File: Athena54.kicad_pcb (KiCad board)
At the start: 4 copper layers, 130.3 x 112.7 mm, 104 parts, among them J1 BATT, J2 HRO_TYPE-C-31-M-12, J3 JTAG_TC2030, J4 RGB, Q1 2N7002, Q2 2N7002, Q3 AO3407, SW1 POWER, SW10 MX Hotswap, SW11 MX Hotswap, SW12 MX Hotswap, SW13 MX Hotswap, SW14 MX Hotswap, SW15 MX Hotswap, SW16 MX Hotswap, SW17 MX Hotswap, SW18 MX Hotswap, SW19 MX Hotswap, SW2 MX Hotswap, SW20 MX Hotswap, SW21 MX Hotswap, SW22 MX Hotswap, SW23 MX Hotswap, SW24 MX Hotswap, SW25 MX Hotswap, SW26 MX Hotswap, SW27 MX Hotswap, SW28 MX Hotswap, SW29 RESET, SW3 MX Hotswap, SW4 MX Hotswap, SW5 MX Hotswap, SW6 MX Hotswap, SW7 MX Hotswap, SW8 MX Hotswap, SW9 MX Hotswap, U1 BQ24075RGT, U2 MAX17048, U3 SRV05-4, U4 MS88SF3

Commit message: fix(schematic): Adjust charging parameters
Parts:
- C6: value 1uF -> 4.7uF
- C7: value 4.7uF -> 1uF
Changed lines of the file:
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@@
       (effects (font (size 0.8 0.8) (thickness 0.15)) (justify mirror))
     )
-    (fp_text value "1uF" (at 0 -1.16) (layer "B.Fab")
+    (fp_text value "4.7uF" (at 0 -1.16) (layer "B.Fab")
       (effects (font (size 1 1) (thickness 0.15)) (justify mirror))
     )
@@
       (effects (font (size 0.8 0.8) (thickness 0.15)) (justify mirror))
     )
-    (fp_text value "4.7uF" (at 0 -1.16) (layer "B.Fab")
+    (fp_text value "1uF" (at 0 -1.16) (layer "B.Fab")
       (effects (font (size 1 1) (thickness 0.15)) (justify mirror))
     )

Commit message: fix(pcb): Update column stagger measurement table
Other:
- board text added: "Pinky2 -> Pinky: 0mm Pinky -> Ring: 5mm Ring -> Middle: 2mm Middle -> Index: 2mm Index -> Index2: 2mm"
- board text removed: "Pinky2 -> Pinky: 0mm Pinky -> Ring: 5mm Ring -> Middle: 1mm Middle -> Index: 2mm Index -> Index2: 2mm"
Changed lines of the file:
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@@
     (fp_line (start 4.47 3.65) (end -4.47 3.65) (layer "B.Fab") (width 0.1))
     (fp_line (start 4.47 -3.65) (end -4.47 -3.65) (layer "B.Fab") (width 0.1))
-    (fp_line (start 4.47 -3.65) (end 4.47 3.65) (layer "F.Fab") (width 0.1))
-    (fp_line (start -4.47 -3.65) (end 4.47 -3.65) (layer "F.Fab") (width 0.1))
     (fp_line (start -4.47 3.65) (end 4.47 3.65) (layer "F.Fab") (width 0.1))
+    (fp_line (start -4.47 -3.65) (end 4.47 -3.65) (layer "F.Fab") (width 0.1))
+    (fp_line (start 4.47 -3.65) (end 4.47 3.65) (layer "F.Fab") (width 0.1))
     (fp_line (start -4.47 -3.65) (end -4.47 3.65) (layer "F.Fab") (width 0.1))
     (pad "" np_thru_hole circle (at 2.89 -2.6 90) (size 0.65 0.65) (drill 0.65) (layers *.Cu *.Mask))
@@
     (effects (font (size 1 1) (thickness 0.2)) (justify left))
   )
-  (gr_text "Pinky2	-> 	Pinky:	0mm\nPinky 	-> 	Ring:	5mm\nRing 	-> 	Middle:	1mm\nMiddle 	-> 	Index:	2mm\nIndex 	-> 	Index2:	2mm\n" (at -13.675 100.025) (layer "Cmts.User")
+  (gr_text "Pinky2	-> 	Pinky:	0mm\nPinky 	-> 	Ring:	5mm\nRing 	-> 	Middle:	2mm\nMiddle 	-> 	Index:	2mm\nIndex 	-> 	Index2:	2mm\n" (at -13.675 100.025) (layer "Cmts.User")
     (effects (font (size 1.5 1.5) (thickness 0.3)) (justify left))
   )

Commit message: fix(schematic): Fix links to footprints
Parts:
- H1, H2, H3, H4, H5: value MountingHole -> 4.3mm
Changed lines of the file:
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@@
       (effects (font (size 1 1) (thickness 0.15)))
     )
-    (fp_text value "MountingHole" (at 0 5.3) (layer "F.Fab")
+    (fp_text value "4.3mm" (at 0 5.3) (layer "F.Fab")
       (effects (font (size 1 1) (thickness 0.15)))
     )
@@
       (effects (font (size 1 1) (thickness 0.15)))
     )
-    (fp_text value "MountingHole" (at 0 5.3) (layer "F.Fab")
+    (fp_text value "4.3mm" (at 0 5.3) (layer "F.Fab")
       (effects (font (size 1 1) (thickness 0.15)))
     )
@@
       (effects (font (size 1 1) (thickness 0.15)))
     )
-    (fp_text value "MountingHole" (at 0 5.3 90) (layer "F.Fab")
+    (fp_text value "4.3mm" (at 0 5.3 90) (layer "F.Fab")
       (effects (font (size 1 1) (thickness 0.15)))
     )
@@
       (effects (font (size 1 1) (thickness 0.15)))
     )
-    (fp_text value "MountingHole" (at 0 5.3) (layer "F.Fab")
+    (fp_text value "4.3mm" (at 0 5.3) (layer "F.Fab")
       (effects (font (size 1 1) (thickness 0.15)))
     )
@@
       (effects (font (size 1 1) (thickness 0.15)))
     )
-    (fp_text value "MountingHole" (at 0 5.3) (layer "F.Fab")
+    (fp_text value "4.3mm" (at 0 5.3) (layer "F.Fab")
       (effects (font (size 1 1) (thickness 0.15)))
     )

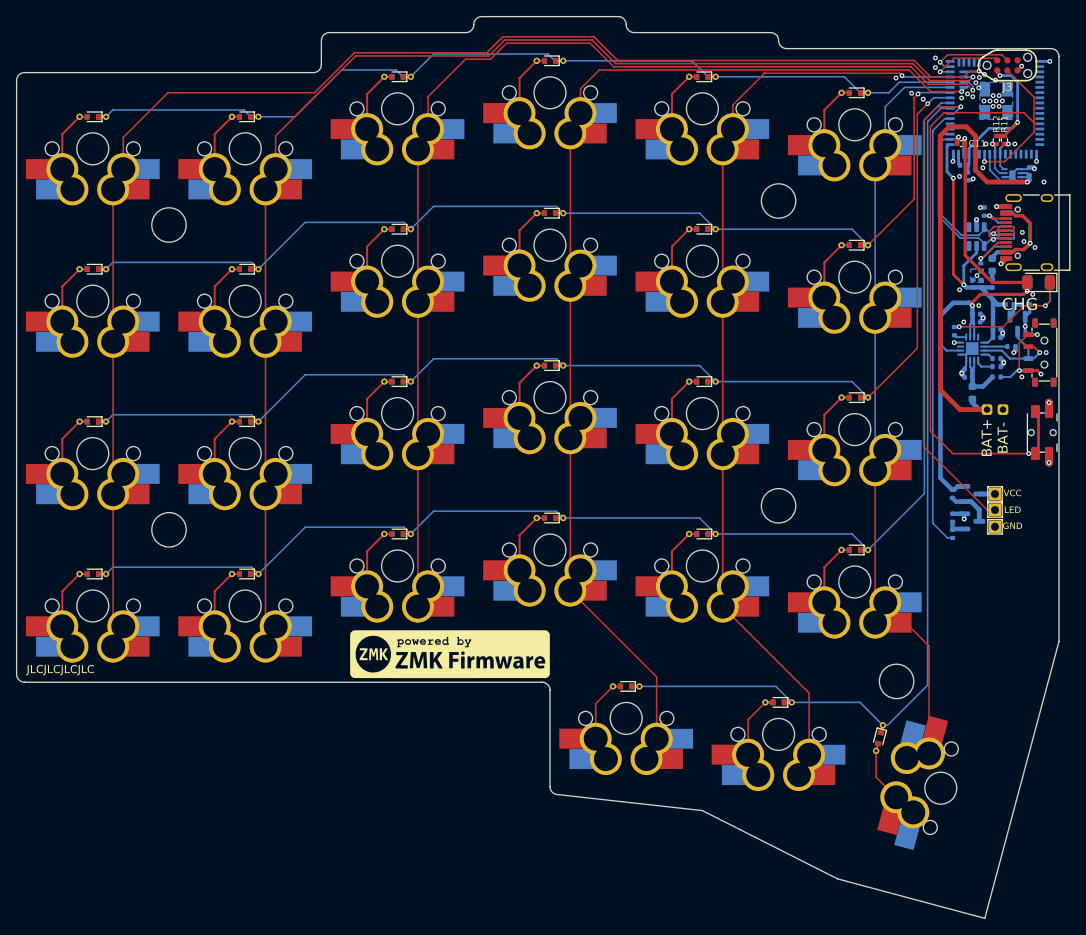
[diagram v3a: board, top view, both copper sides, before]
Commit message: fix(pcb): Add fillet to thumb cluster edge cut
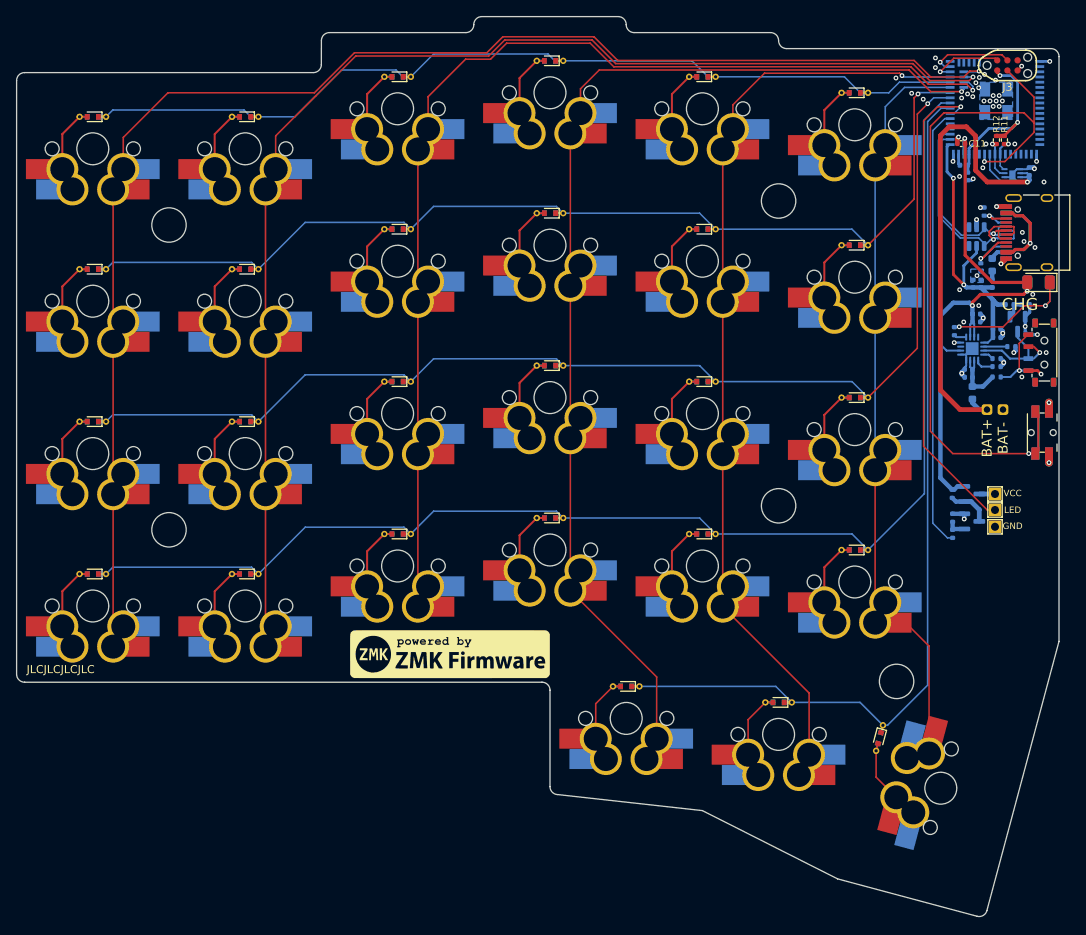
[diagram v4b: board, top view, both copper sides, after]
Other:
- board size 130.3 x 112.7 mm -> 130.3 x 112.5 mm
